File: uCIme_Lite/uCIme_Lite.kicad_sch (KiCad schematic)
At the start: 9 parts

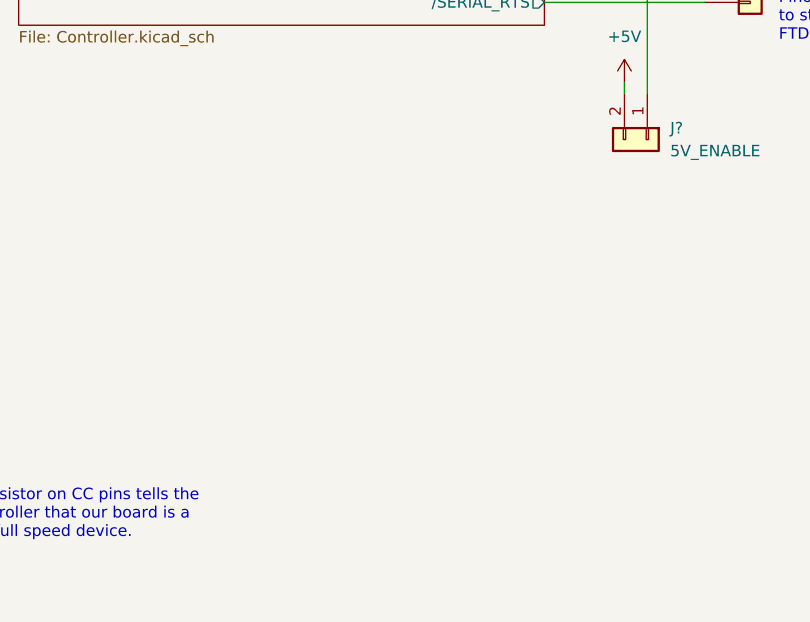
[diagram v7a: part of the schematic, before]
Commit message: lite: Added a led that lights when PC USB connector is plugged.
Signed-off-by: Adrien Ricciardi <aricciardi@baylibre.com>
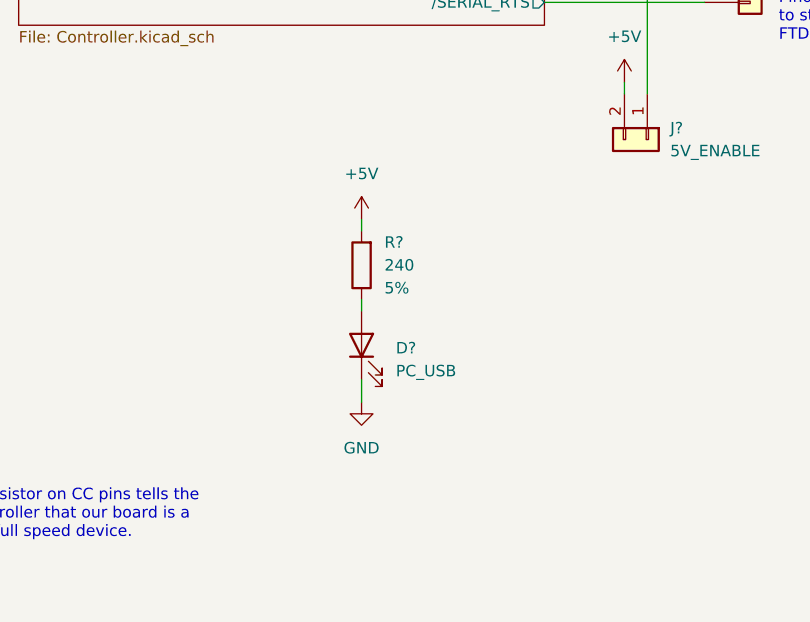
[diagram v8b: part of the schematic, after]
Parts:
- added D?: PC_USB, symbol Device:LED
- added R?: 240, Resistor_SMD:R_1206_3216Metric, symbol Device:R
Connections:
- net +5V: now also R?.2
- net GND: now also D?.1 (K)
- new net: D?.2 (A), R?.1
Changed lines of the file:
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@@
+    (stroke (width 0) (type default) (color 0 0 0 0))
+  )
+  (wire (pts (xy 154.94 140.97) (xy 154.94 139.7))
     (stroke (width 0) (type default) (color 0 0 0 0))
   )
@@
     (stroke (width 0) (type default) (color 0 0 0 0))
   )
+  (wire (pts (xy 154.94 157.48) (xy 154.94 160.02))
+    (stroke (width 0) (type default) (color 0 0 0 0))
+  )
   (wire (pts (xy 54.61 137.16) (xy 62.23 137.16))
     (stroke (width 0) (type default) (color 0 0 0 0))
@@
   )
   (wire (pts (xy 71.12 35.56) (xy 71.12 36.83))
+    (stroke (width 0) (type default) (color 0 0 0 0))
+  )
+  (wire (pts (xy 154.94 149.86) (xy 154.94 148.59))
     (stroke (width 0) (type default) (color 0 0 0 0))
   )
@@
   (label "SSRX1_N" (at 259.08 78.74 180)
     (effects (font (size 1.27 1.27)) (justify right bottom))
+  )
+  (symbol (lib_id "Device:LED") (at 154.94 153.67 90) (unit 1)
+    (in_bom yes) (on_board yes) (fields_autoplaced)
+    (property "Reference" "D?" (id 0) (at 158.75 153.9874 90)
+      (effects (font (size 1.27 1.27)) (justify right))
+    )
+    (property "Value" "PC_USB" (id 1) (at 158.75 156.5274 90)
+      (effects (font (size 1.27 1.27)) (justify right))
+    )
+    (property "Footprint" "" (id 2) (at 154.94 153.67 0)
+      (effects (font (size 1.27 1.27)) hide)
+    )
+    (property "Datasheet" "~" (id 3) (at 154.94 153.67 0)
+      (effects (font (size 1.27 1.27)) hide)
+    )
+    (pin "1")
+    (pin "2")
   )
   (symbol (lib_id "PJ-082BH:JACK-C-PC-10A-RA(R)") (at 229.87 26.67 0) (mirror y) (unit 1)
@@
     )
     (property "Datasheet" "" (id 3) (at 184.15 100.33 0)
+      (effects (font (size 1.27 1.27)) hide)
+    )
+    (pin "1")
+  )
+  (symbol (lib_id "power:GND") (at 154.94 160.02 0) (unit 1)
+    (in_bom yes) (on_board yes) (fields_autoplaced)
+    (property "Reference" "#PWR?" (id 0) (at 154.94 166.37 0)
+      (effects (font (size 1.27 1.27)) hide)
+    )
+    (property "Value" "GND" (id 1) (at 154.94 165.1 0))
+    (property "Footprint" "" (id 2) (at 154.94 160.02 0)
+      (effects (font (size 1.27 1.27)) hide)
+    )
+    (property "Datasheet" "" (id 3) (at 154.94 160.02 0)
       (effects (font (size 1.27 1.27)) hide)
     )
@@
     (pin "1")
   )
+  (symbol (lib_id "Device:R") (at 154.94 144.78 180) (unit 1)
+    (in_bom yes) (on_board yes) (fields_autoplaced)
+    (property "Reference" "R?" (id 0) (at 157.48 142.2399 0)
+      (effects (font (size 1.27 1.27)) (justify right))
+    )
+    (property "Value" "240" (id 1) (at 157.48 144.7799 0)
+      (effects (font (size 1.27 1.27)) (justify right))
+    )
+    (property "Footprint" "Resistor_SMD:R_1206_3216Metric" (id 2) (at 156.718 144.78 90)
+      (effects (font (size 1.27 1.27)) hide)
+    )
+    (property "Datasheet" "~" (id 3) (at 154.94 144.78 0)
+      (effects (font (size 1.27 1.27)) hide)
+    )
+    (property "PartNumber" "" (id 4) (at 154.94 144.78 0)
+      (effects (font (size 1.27 1.27)) hide)
+    )
+    (property "Value1" "5%" (id 5) (at 157.48 147.3199 0)
+      (effects (font (size 1.27 1.27)) (justify right))
+    )
+    (pin "1")
+    (pin "2")
+  )
   (symbol (lib_id "power:+5V") (at 62.23 135.89 0) (unit 1)
     (in_bom yes) (on_board yes) (fields_autoplaced)
@@
     (pin "1")
   )
+  (symbol (lib_id "power:+5V") (at 154.94 139.7 0) (unit 1)
+    (in_bom yes) (on_board yes) (fields_autoplaced)
+    (property "Reference" "#PWR?" (id 0) (at 154.94 143.51 0)
+      (effects (font (size 1.27 1.27)) hide)
+    )
+    (property "Value" "+5V" (id 1) (at 154.94 134.62 0))
+    (property "Footprint" "" (id 2) (at 154.94 139.7 0)
+      (effects (font (size 1.27 1.27)) hide)
+    )
+    (property "Datasheet" "" (id 3) (at 154.94 139.7 0)
+      (effects (font (size 1.27 1.27)) hide)
+    )
+    (pin "1")
+  )
   (symbol (lib_id "power:GND") (at 71.12 36.83 0) (unit 1)
     (in_bom yes) (on_board yes) (fields_autoplaced)
@@
       (reference "#PWR?") (unit 1) (value "GND") (footprint "")
     )
+    (path "/1b84b657-1835-43e8-a37b-41694adaf83b"
+      (reference "#PWR?") (unit 1) (value "GND") (footprint "")
+    )
     (path "/85cb8885-4077-4bc3-b1fe-5b247ce2fc7e/1e62cbd4-c369-40dd-ab47-a229c3ace3e2"
       (reference "#PWR?") (unit 1) (value "GND") (footprint "")
@@
       (reference "#PWR?") (unit 1) (value "GND") (footprint "")
     )
+    (path "/d1f5c512-52fa-4225-b07a-e5070d38a7b0"
+      (reference "#PWR?") (unit 1) (value "+5V") (footprint "")
+    )
     (path "/85cb8885-4077-4bc3-b1fe-5b247ce2fc7e/d2c282de-155e-470e-a5c7-4f48b6f4c506"
       (reference "#PWR?") (unit 1) (value "GND") (footprint "")
@@
       (reference "C?") (unit 1) (value "1u") (footprint "Capacitor_SMD:C_0603_1608Metric")
     )
+    (path "/00595cf1-fd6c-46ee-920b-e961271cd227"
+      (reference "D?") (unit 1) (value "PC_USB") (footprint "")
+    )
     (path "/b72074d7-db6e-4ce2-896d-216adccf1d19/73043a3f-e53c-4ce8-8715-61c731acbb9d"
       (reference "D?") (unit 1) (value "POWER_SWITCH") (footprint "")
@@
       (reference "R?") (unit 1) (value "240") (footprint "Resistor_SMD:R_1206_3216Metric")
     )
+    (path "/5feff8ad-b588-452b-b2cd-506cadfa8623"
+      (reference "R?") (unit 1) (value "240") (footprint "Resistor_SMD:R_1206_3216Metric")
+    )
